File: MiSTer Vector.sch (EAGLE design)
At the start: 49 parts, among them CON2 22-23-2021, IC1 74HC00D, IC2 TL084, IC3 TL084, IC7 MAX6105, U1 MCP4922, U2 MCP4922, U3 MCP4922, U8 VASD1-SIP, X2 ILDA 25 Pin

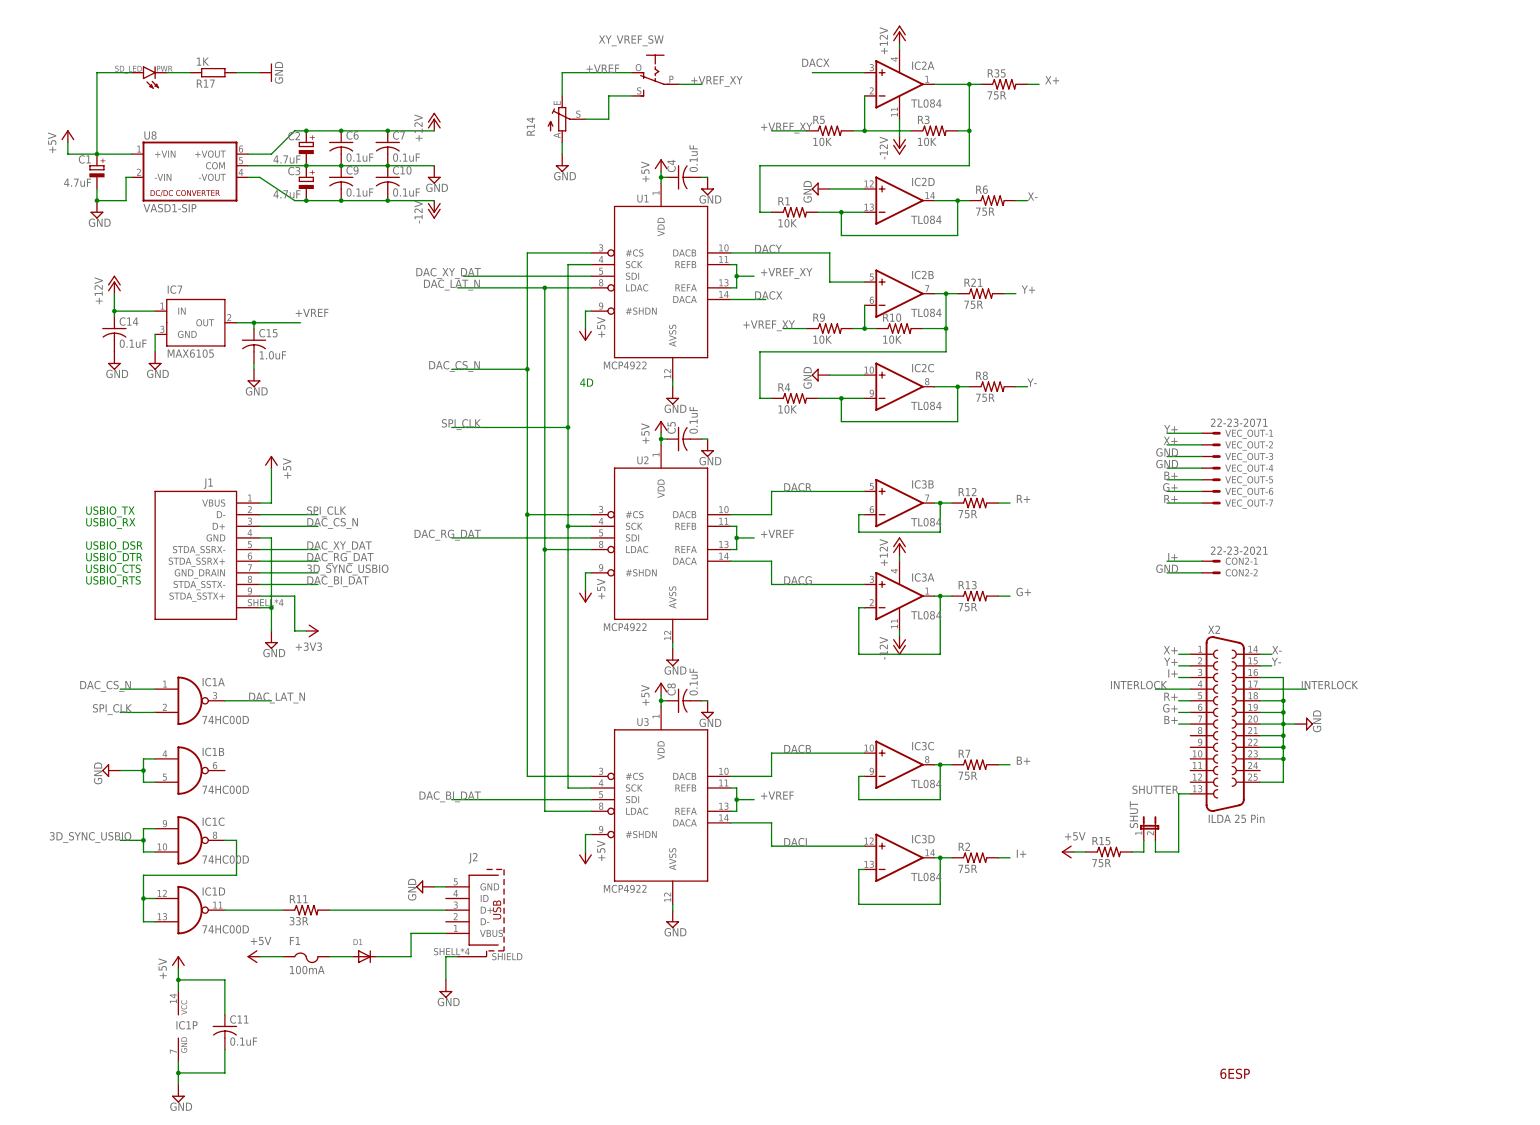
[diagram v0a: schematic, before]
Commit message: added size adjustment for Molex output. ILDA fixed to 0-5V
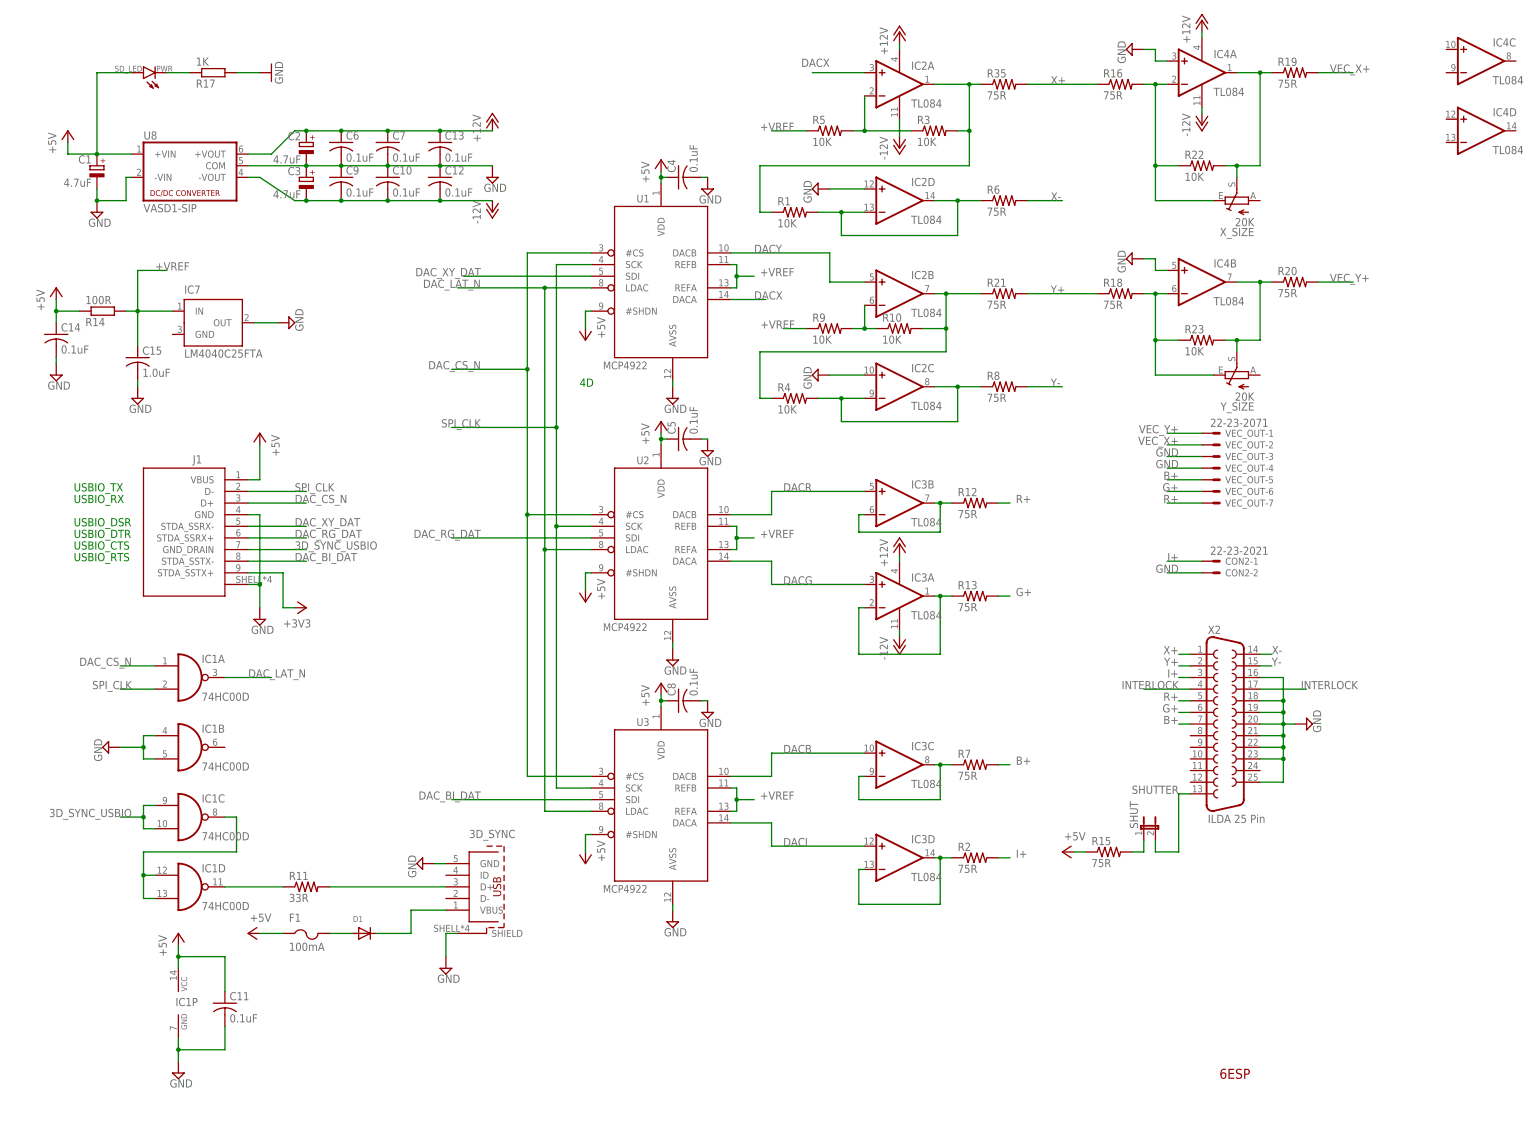
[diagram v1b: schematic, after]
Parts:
- removed J2: (no value), 632723100011_Eagle_WR-USB_rev19b:65100516121
- removed XY_VREF_SW: (no value), adafruit:EG1218S
- added 3D_SYNC: (no value), 632723100011_Eagle_WR-USB_rev19b:65100516121
- added C12, C13: 0.1uF, adafruit:C-USC0603
- added IC4: TL084, favreau:TL084
- added R16, R18, R19, R20: 75R, resistor:R-US_R0603
- added R22, R23: 10K, resistor:R-US_R0603
- added X_SIZE, Y_SIZE: 20K, pot:TRIM_EU-B25P
- IC7: value MAX6105 -> LM4040C25FTA
- R14: value (none) -> 100R; device pot:TRIM_EU-B25P -> rcl:R-EU_R0603
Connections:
- removed net +VREF_XY: R5.1, R9.1, U1.REFA, U1.REFB, XY_VREF_SW.P
- removed net N$13: R14.S, XY_VREF_SW.S
- new net N$14: IC4A.-IN, R16.2, R22.1, X_SIZE.E
- new net N$15: IC4B.-IN, R18.2, R23.1, Y_SIZE.E
- new net N$16: IC4B.OUT, R20.1, R23.2, Y_SIZE.S
- new net N$17: IC4A.OUT, R19.1, R22.2, X_SIZE.S
- new net VEC_X+: R19.2, VEC_OUT-2.S
- new net VEC_Y+: R20.2, VEC_OUT-1.S
- net +12V: now also C13.1, IC4A.V+; no longer C14.1, IC7.IN
- net +5V: now also C14.1, R14.1
- net +VREF: now also IC7.IN, R14.2, R5.1, R9.1, U1.REFA, U1.REFB; no longer IC7.OUT, R14.E, XY_VREF_SW.O
- net -12V: now also C12.2, IC4A.V-
- net GND: now also 3D_SYNC.GND, 3D_SYNC.SHIELD, C12.1, C13.2, IC4A.+IN, IC4B.+IN, IC7.OUT; no longer IC7.GND, J2.GND, J2.SHIELD, R14.A
- net N$6: now also 3D_SYNC.VBUS; no longer J2.VBUS
- net N$9: now also 3D_SYNC.D+; no longer J2.D+
- net X+: now also R16.1; no longer VEC_OUT-2.S
- net Y+: now also R18.1; no longer VEC_OUT-1.S
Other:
- moved on the sheet: C11, C14, C15, D1, F1, IC1A, IC1B, IC1C, IC1D, IC1P, IC7, J1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

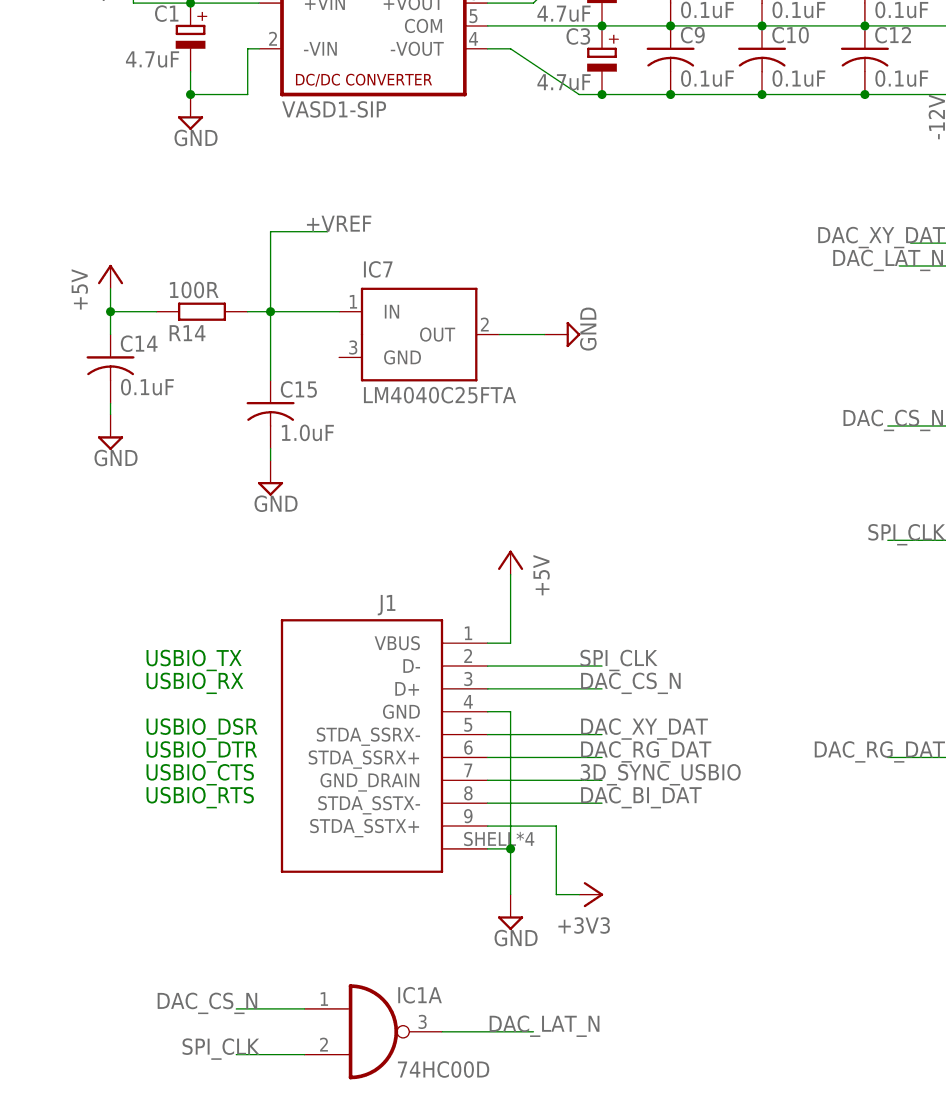
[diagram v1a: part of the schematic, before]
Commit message: swapped USBIO TX/RX pairs, as done in most USB3 TypeA-TypeA cables
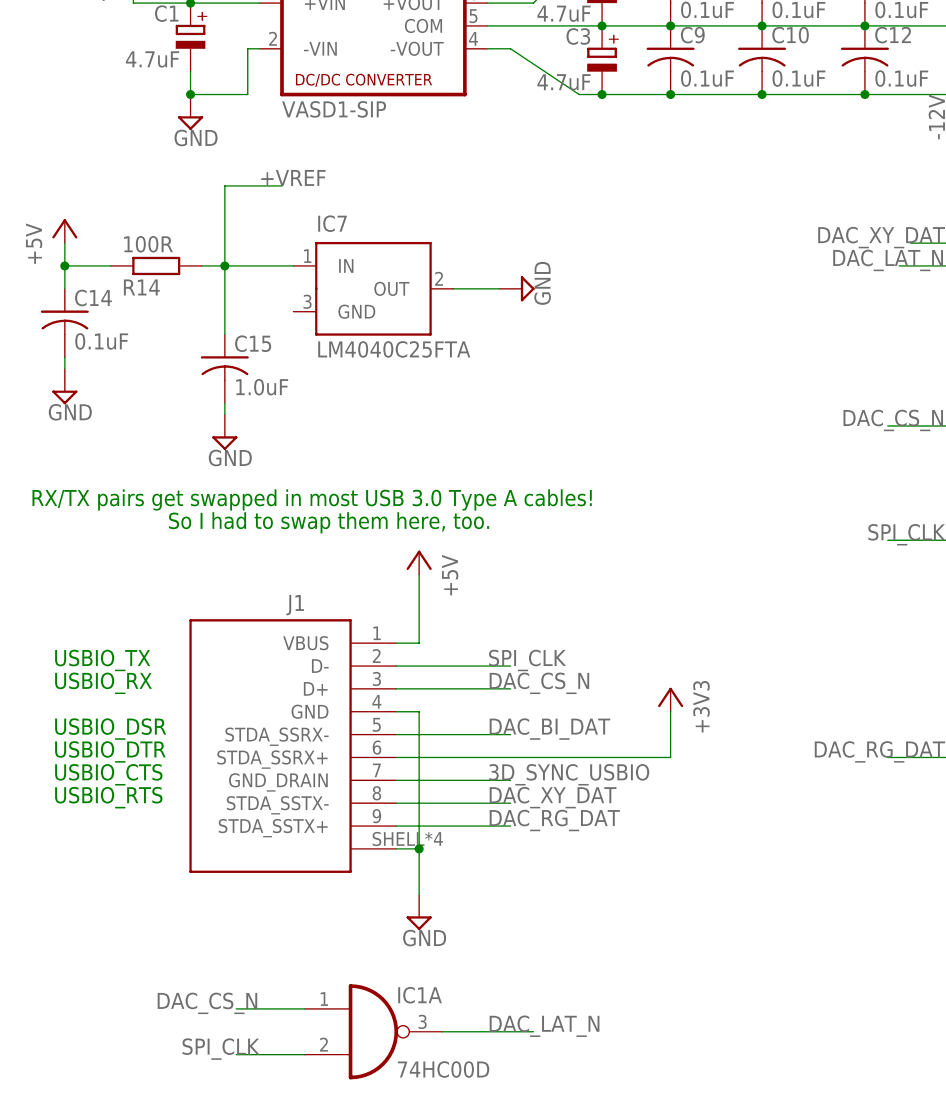
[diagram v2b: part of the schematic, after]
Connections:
- net +3V3: now also J1.STDA_SSRX+; no longer J1.STDA_SSTX+
- net DAC_BI_DAT: now also J1.STDA_SSRX-; no longer J1.STDA_SSTX-
- net DAC_RG_DAT: now also J1.STDA_SSTX+; no longer J1.STDA_SSRX+
- net DAC_XY_DAT: now also J1.STDA_SSTX-; no longer J1.STDA_SSRX-
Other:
- note added: "RX/TX pairs get swapped in most USB 3.0 Type A cables!"
- note added: "So I had to swap them here, too."
- moved on the sheet: C14, C15, IC7, J1, R14
